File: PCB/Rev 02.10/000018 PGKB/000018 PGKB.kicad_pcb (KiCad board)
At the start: 4 copper layers, 93.5 x 72.5 mm, 156 parts, among them J1 USB C, J2 S4B-PH-SM4-TB, U1 SN74HCS365PWR, U2 SN74HCS365PWR, U3 SN74HCS365PWR, U4 W25Q80DVSSIG, U5 RP2040, U6 MCP1825T-3302E/DC, U7 CAT811TTBI-GT3, Y1 12 MHz

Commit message: Signals renamed
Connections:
- net /Main/Microcontroller/GPIO12 renamed /Main/Microcontroller/GPIO29
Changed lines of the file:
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@@
 	(net 39 "unconnected-(J1-SBU2-PadB8)")
 	(net 40 "/Main/Microcontroller/NEOPIX_DRIVE")
-	(net 41 "/Main/Microcontroller/GPIO12")
+	(net 41 "/Main/Microcontroller/GPIO29")
 	(net 42 "/Main/Buttons/Button6")
 	(net 43 "/Main/Buttons/Button7")
@@
 		(fp_arc
 			(start 1.31605 -0.683114)
-			(mid 1.907695 -0.405492)
+			(mid 1.907699 -0.405492)
 			(end 2.078018 0.225468)
 			(stroke
@@
 		(fp_arc
 			(start 1.372869 0.972724)
-			(mid 0.966366 0.781547)
+			(mid 0.966362 0.781547)
 			(end 0.82295 0.35584)
 			(stroke
@@
 		(fp_arc
 			(start 3.12764 1.232463)
-			(mid 2.61934 1.092397)
+			(mid 2.619347 1.092399)
 			(end 2.369218 0.628268)
 			(stroke
@@
 		(fp_arc
 			(start 5.03409 0.259459)
-			(mid 5.191951 -0.372877)
+			(mid 5.19195 -0.37288)
 			(end 5.765118 -0.683118)
 			(stroke
@@
 		(fp_arc
 			(start 6.280538 1.013814)
-			(mid 6.045436 1.181019)
+			(mid 6.045436 1.181008)
 			(end 5.761568 1.232468)
 			(stroke
@@
 		(fp_arc
 			(start 7.407765 -0.124568)
-			(mid 7.589655 -0.340729)
+			(mid 7.589656 -0.340694)
 			(end 7.859781 -0.423381)
 			(stroke
@@
 		(fp_arc
 			(start 7.955657 -0.683113)
-			(mid 8.404805 -0.489301)
+			(mid 8.404847 -0.489303)
 			(end 8.54819 -0.02159)
 			(stroke
@@
 		(fp_arc
 			(start 9.708398 -0.423378)
-			(mid 9.968762 -0.344292)
+			(mid 9.96879 -0.344297)
 			(end 10.097 -0.104281)
 			(stroke
@@
 		(fp_arc
 			(start 9.71855 1.232464)
-			(mid 9.210242 1.092402)
+			(mid 9.21027 1.092398)
 			(end 8.960131 0.628268)
 			(stroke
@@
 			(layers "B.Cu" "B.Paste" "B.Mask")
 			(roundrect_rratio 0.25)
-			(net 41 "/Main/Microcontroller/GPIO12")
+			(net 41 "/Main/Microcontroller/GPIO29")
 			(pinfunction "O2")
 			(pintype "tri_state")
@@
 			(layers "B.Cu" "B.Paste" "B.Mask")
 			(roundrect_rratio 0.25)
-			(net 41 "/Main/Microcontroller/GPIO12")
+			(net 41 "/Main/Microcontroller/GPIO29")
 			(pinfunction "GPIO29_ADC3")
 			(pintype "bidirectional")

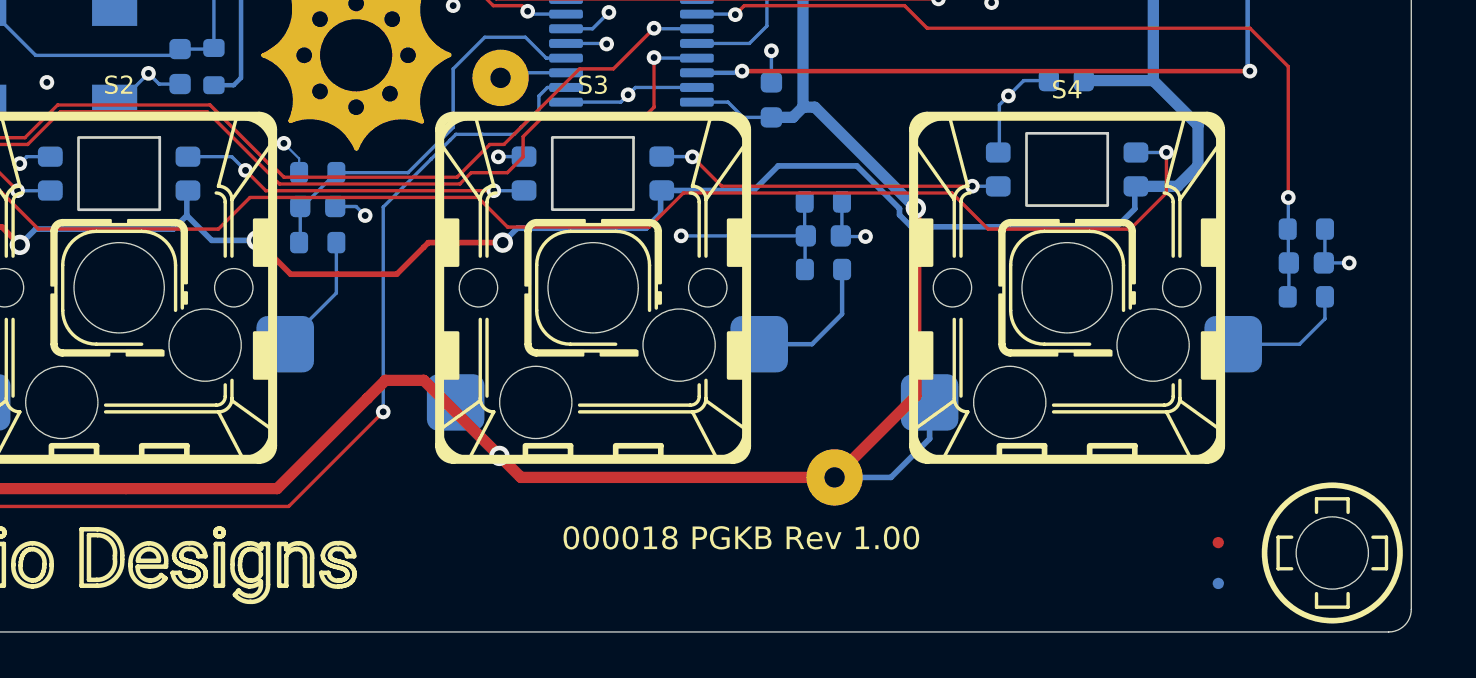
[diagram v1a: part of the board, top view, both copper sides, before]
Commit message: GND hook added
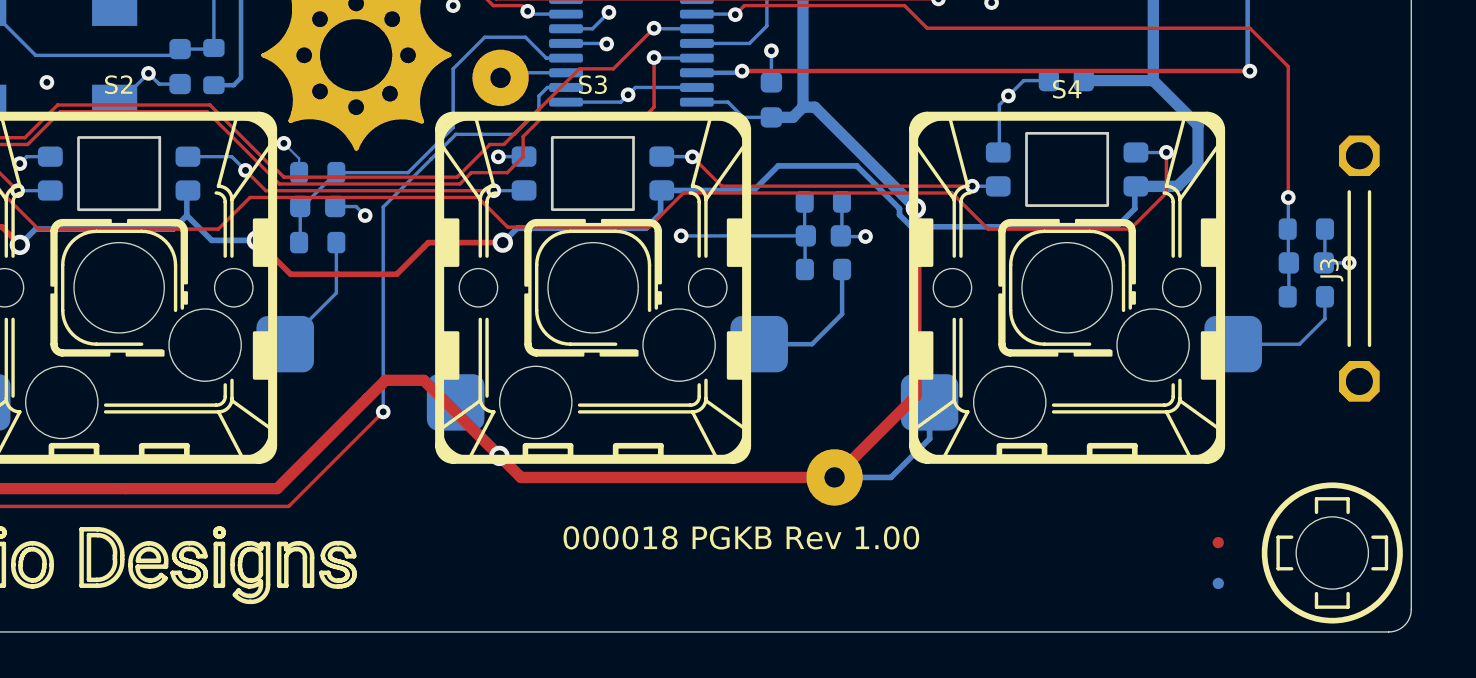
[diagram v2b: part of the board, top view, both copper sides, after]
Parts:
- added J3: GND Hook, KD_Connector_Pads:GND_HOOK_M, F.Cu at (133.8, 159.7)
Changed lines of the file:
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@@
 	(net 113 "unconnected-(J2-PadMP2)")
 	(net 114 "unconnected-(J2-PadMP1)")
+	(net 115 "unconnected-(J3-Pin_1-Pad1)")
+	(net 116 "unconnected-(J3-Pin_1-Pad2)")
 	(footprint "KD_Mechanical_Mounting_Hole:PTH_3.2mm_M3_clearance_B"
 		(layer "F.Cu")
@@
 		(fp_arc
 			(start 1.31605 -0.683114)
-			(mid 1.907699 -0.405492)
+			(mid 1.907695 -0.405492)
 			(end 2.078018 0.225468)
 			(stroke
@@
 		(fp_arc
 			(start 1.372869 0.972724)
-			(mid 0.966362 0.781547)
+			(mid 0.96636 0.78155)
 			(end 0.82295 0.35584)
 			(stroke
@@
 		(fp_arc
 			(start 3.12764 1.232463)
-			(mid 2.619347 1.092399)
+			(mid 2.61934 1.092397)
 			(end 2.369218 0.628268)
 			(stroke
@@
 		(fp_arc
 			(start 5.03409 0.259459)
-			(mid 5.19195 -0.37288)
+			(mid 5.191951 -0.372877)
 			(end 5.765118 -0.683118)
 			(stroke
@@
 		(fp_arc
 			(start 6.280538 1.013814)
-			(mid 6.045436 1.181008)
+			(mid 6.045436 1.181019)
 			(end 5.761568 1.232468)
 			(stroke
@@
 		(fp_arc
 			(start 7.407765 -0.124568)
-			(mid 7.589656 -0.340694)
+			(mid 7.589655 -0.340729)
 			(end 7.859781 -0.423381)
 			(stroke
@@
 		(fp_arc
 			(start 7.955657 -0.683113)
-			(mid 8.404847 -0.489303)
+			(mid 8.404805 -0.489301)
 			(end 8.54819 -0.02159)
 			(stroke
@@
 		(fp_arc
 			(start 9.708398 -0.423378)
-			(mid 9.96879 -0.344297)
+			(mid 9.968762 -0.344292)
 			(end 10.097 -0.104281)
 			(stroke
@@
 		(fp_arc
 			(start 9.71855 1.232464)
-			(mid 9.21027 1.092398)
+			(mid 9.210242 1.092402)
 			(end 8.960131 0.628268)
 			(stroke
@@
 		)
 	)
+	(footprint "KD_Connector_Pads:GND_HOOK_M"
+		(layer "F.Cu")
+		(at 133.85 159.65 90)
+		(property "Reference" "J3"
+			(at 0 -1.3 90)
+			(layer "F.SilkS")
+			(effects
+				(font
+					(size 0.8 0.8)
+					(thickness 0.15)
+				)
+			)
+		)
+		(property "Value" "GND Hook"
+			(at 0 0 90)
+			(layer "F.Fab")
+			(hide yes)
+			(effects
+				(font
+					(size 0.8 0.8)
+					(thickness 0.15)
+				)
+			)
+		)
+		(property "Footprint" "KD_Connector_Pads:GND_HOOK_M"
+			(at 0 0 90)
+			(layer "F.Fab")
+			(hide yes)
+			(effects
+				(font
+					(size 1.27 1.27)
+					(thickness 0.15)
+				)
+			)
+		)
+		(property "Datasheet" ""
+			(at 0 0 90)
+			(layer "F.Fab")
+			(hide yes)
+			(effects
+				(font
+					(size 1.27 1.27)
+					(thickness 0.15)
+				)
+			)
+		)
+		(property "Description" "Oscilloscope probe GND hook"
+			(at 0 0 90)
+			(layer "F.Fab")
+			(hide yes)
+			(effects
+				(font
+					(size 1.27 1.27)
+					(thickness 0.15)
+				)
+			)
+		)
+		(property "Manufacturer" "DNP"
+			(at 0 0 90)
+			(unlocked yes)
+			(layer "F.Fab")
+			(hide yes)
+			(effects
+				(font
+					(size 1 1)
+					(thickness 0.15)
+				)
+			)
+		)
+		(property "MFG_PartNo" "DNP"
+			(at 0 0 90)
+			(unlocked yes)
+			(layer "F.Fab")
+			(hide yes)
+			(effects
+				(font
+					(size 1 1)
+					(thickness 0.15)
+				)
+			)
+		)
+		(property "Supplier" "DNP"
+			(at 0 0 90)
+			(unlocked yes)
+			(layer "F.Fab")
+			(hide yes)
+			(effects
+				(font
+					(size 1 1)
+					(thickness 0.15)
+				)
+			)
+		)
+		(property "Supplier_PartNo" "DNP"
+			(at 0 0 90)
+			(unlocked yes)
+			(layer "F.Fab")
+			(hide yes)
+			(effects
+				(font
+					(size 1 1)
+					(thickness 0.15)
+				)
+			)
+		)
+		(property "DNP" "T"
+			(at 0 0 90)
+			(unlocked yes)
+			(layer "F.Fab")
+			(hide yes)
+			(effects
+				(font
+					(size 1 1)
+					(thickness 0.15)
+				)
+			)
+		)
+		(property "Price" "0.00"
+			(at 0 0 90)
+			(unlocked yes)
+			(layer "F.Fab")
+			(hide yes)
+			(effects
+				(font
+					(size 1 1)
+					(thickness 0.15)
+				)
+			)
+		)
+		(property ki_fp_filters "1x01")
+		(sheetname "Mechanical")
+		(sheetfile "mechanical.kicad_sch")
+		(fp_line
+			(start -3.4 -0.45)
+			(end 3.4 -0.45)
+			(stroke
+				(width 0.15)
+				(type solid)
+			)
+			(layer "F.SilkS")
+		)
+		(fp_line
+			(start 3.4 0.45)
+			(end -3.4 0.45)
+			(stroke
+				(width 0.15)
+				(type solid)
+			)
+			(layer "F.SilkS")
+		)
+		(fp_text user "GND"
+			(at 0 0.05 90)
+			(layer "F.Fab")
+			(hide yes)
+			(effects
+				(font
+					(size 0.44 0.44)
+					(thickness 0.06)
+				)
+			)
+		)
+		(pad "1" thru_hole roundrect
+			(at -5 0 90)
+			(size 1.8 1.8)
+			(drill 1.2)
+			(layers "*.Cu" "*.Mask")
+			(remove_unused_layers no)
+			(roundrect_rratio 0.25)
+			(chamfer_ratio 0.25)
+			(chamfer top_left top_right bottom_left bottom_right)
+			(net 115 "unconnected-(J3-Pin_1-Pad1)")
+			(pinfunction "Pin_1")
+			(pintype "passive")
+			(solder_mask_margin 0.0508)
+		)
+		(pad "2" thru_hole roundrect
+			(at 5 0 90)
+			(size 1.8 1.8)
+			(drill 1.2)
+			(layers "*.Cu" "*.Mask")
+			(remove_unused_layers no)
+			(roundrect_rratio 0.25)
+			(chamfer_ratio 0.25)
+			(chamfer top_left top_right bottom_left bottom_right)
+			(net 116 "unconnected-(J3-Pin_1-Pad2)")
+			(pinfunction "Pin_1")
+			(pintype "passive")
+			(solder_mask_margin 0.0508)
+		)
+	)
